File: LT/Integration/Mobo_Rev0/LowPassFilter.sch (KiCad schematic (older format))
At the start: 5 parts

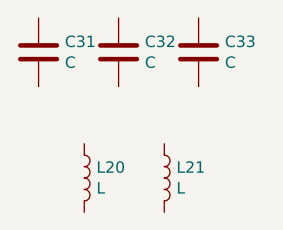
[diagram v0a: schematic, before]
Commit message: I uploaded the schematics for the receiving stage into their respective hierarchial sheets and have begun the integration of the received stage
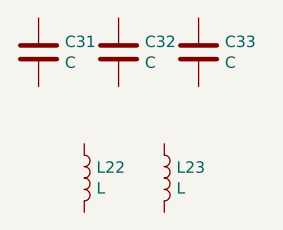
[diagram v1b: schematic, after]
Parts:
- C31, C32, C33: footprint Capacitor_SMD:C_0805_2012Metric -> (none)
- L22: renamed from L20; footprint Inductor_SMD:L_0805_2012Metric -> (none)
- L23: renamed from L21; footprint Inductor_SMD:L_0805_2012Metric -> (none)
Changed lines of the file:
@@
 F 0 "C31" H 4215 1946 50  0000 L CNN
 F 1 "C" H 4215 1855 50  0000 L CNN
-F 2 "Capacitor_SMD:C_0805_2012Metric" H 4138 1750 50  0001 C CNN
+F 2 "" H 4138 1750 50  0001 C CNN
 F 3 "~" H 4100 1900 50  0001 C CNN
 	1    4100 1900
@@
 F 0 "C32" H 4565 1946 50  0000 L CNN
 F 1 "C" H 4565 1855 50  0000 L CNN
-F 2 "Capacitor_SMD:C_0805_2012Metric" H 4488 1750 50  0001 C CNN
+F 2 "" H 4488 1750 50  0001 C CNN
 F 3 "~" H 4450 1900 50  0001 C CNN
 	1    4450 1900
@@
 F 0 "C33" H 4915 1946 50  0000 L CNN
 F 1 "C" H 4915 1855 50  0000 L CNN
-F 2 "Capacitor_SMD:C_0805_2012Metric" H 4838 1750 50  0001 C CNN
+F 2 "" H 4838 1750 50  0001 C CNN
 F 3 "~" H 4800 1900 50  0001 C CNN
 	1    4800 1900
@@
 $EndComp
 $Comp
-L Device:L L20
+L Device:L L22
 U 1 1 5E4C472F
 P 4300 2450
-F 0 "L20" H 4353 2496 50  0000 L CNN
+F 0 "L22" H 4353 2496 50  0000 L CNN
 F 1 "L" H 4353 2405 50  0000 L CNN
-F 2 "Inductor_SMD:L_0805_2012Metric" H 4300 2450 50  0001 C CNN
+F 2 "" H 4300 2450 50  0001 C CNN
 F 3 "~" H 4300 2450 50  0001 C CNN
 	1    4300 2450
@@
 $EndComp
 $Comp
-L Device:L L21
+L Device:L L23
 U 1 1 5E4C477A
 P 4650 2450
-F 0 "L21" H 4703 2496 50  0000 L CNN
+F 0 "L23" H 4703 2496 50  0000 L CNN
 F 1 "L" H 4703 2405 50  0000 L CNN
-F 2 "Inductor_SMD:L_0805_2012Metric" H 4650 2450 50  0001 C CNN
+F 2 "" H 4650 2450 50  0001 C CNN
 F 3 "~" H 4650 2450 50  0001 C CNN
 	1    4650 2450

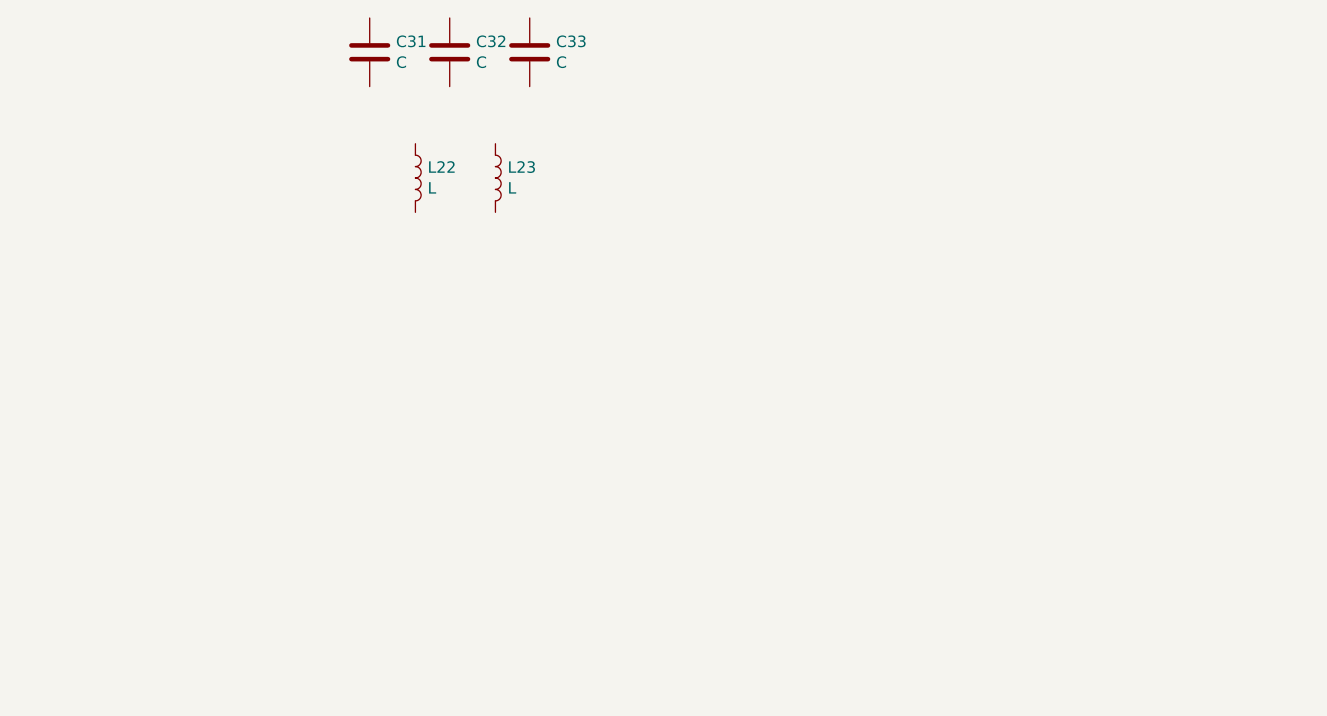
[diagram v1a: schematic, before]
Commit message: Finished a preliminary layout for the Receiving Stage, and uploaded the schematics for the Pre-Amp, 29.4 BPF, and 29.4 LPF.
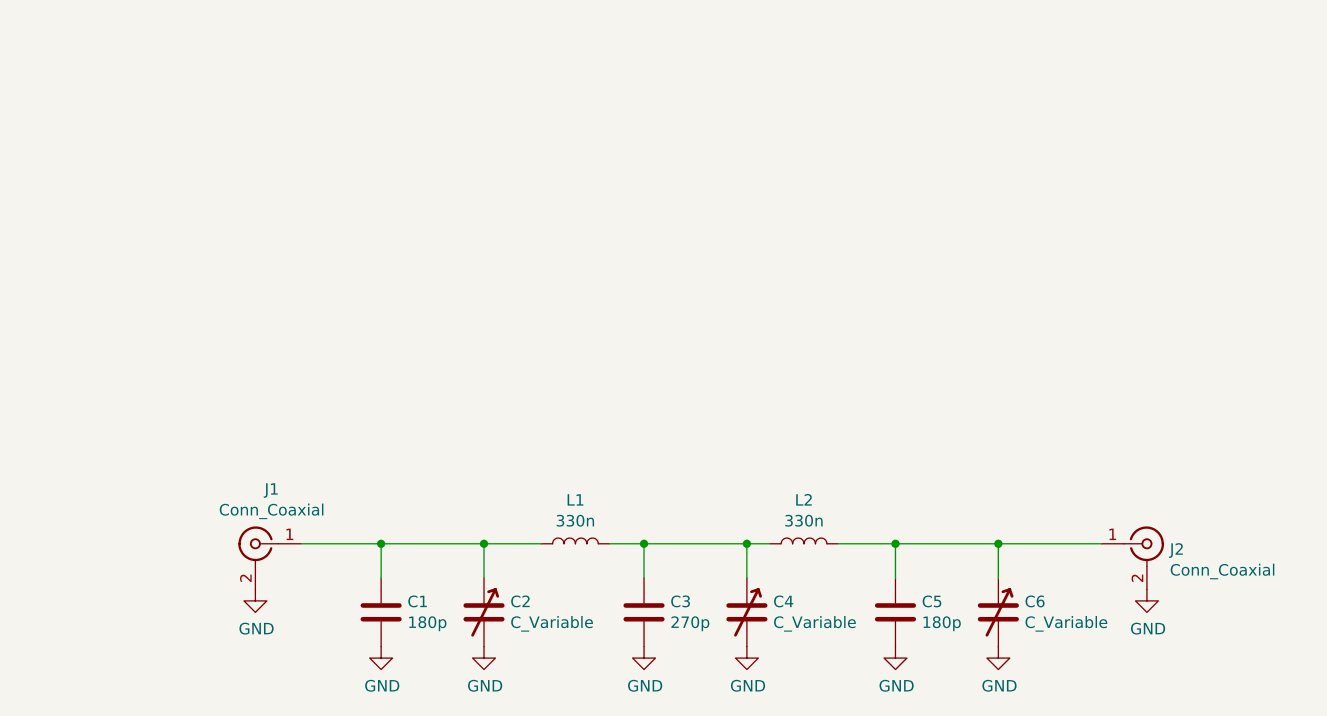
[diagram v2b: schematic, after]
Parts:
- removed C31, C32, C33: C, symbol Device:C
- removed L22, L23: L, symbol Device:L
- added C1, C5: 180p, Capacitor_SMD:C_0805_2012Metric_Pad1.15x1.40mm_HandSolder, symbol Device:C
- added C2, C4, C6: C_Variable, LT:CAP_Trimmer_TZB4Z, symbol Device:C_Variable
- added C3: 270p, Capacitor_SMD:C_0805_2012Metric_Pad1.15x1.40mm_HandSolder, symbol Device:C
- added J1, J2: Conn_Coaxial, Connector_Coaxial:SMA_Molex_73251-1153_EdgeMount_Horizontal, symbol Connector:Conn_Coaxial
- added L1, L2: 330n, Inductor_SMD:L_0805_2012Metric_Pad1.15x1.40mm_HandSolder, symbol Device:L
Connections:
- new net: C1.1, C2.1, J1.1 (In), L1.1
- new net: C3.1, C4.1, L1.2, L2.1
- new net: C5.1, C6.1, J2.1 (In), L2.2
- new net GND: C1.2, C2.2, C3.2, C4.2, C5.2, C6.2, J1.2 (Ext), J2.2 (Ext)

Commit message: Annotating components for Transmitting stage. In progress
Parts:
- renumbered C1 to C40, C2 to C41, C3 to C42, C4 to C43, C5 to C44, C6 to C45
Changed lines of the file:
@@
 $EndComp
 $Comp
-L Device:C C1
+L Device:C C40
 U 1 1 5E1FE5C6
 P 4150 4350
-F 0 "C1" H 4265 4396 50  0000 L CNN
+F 0 "C40" H 4265 4396 50  0000 L CNN
 F 1 "180p" H 4265 4305 50  0000 L CNN
 F 2 "Capacitor_SMD:C_0805_2012Metric_Pad1.15x1.40mm_HandSolder" H 4188 4200 50  0001 C CNN
@@
 $EndComp
 $Comp
-L Device:C C3
+L Device:C C42
 U 1 1 5E201B6F
 P 5300 4350
-F 0 "C3" H 5415 4396 50  0000 L CNN
+F 0 "C42" H 5415 4396 50  0000 L CNN
 F 1 "270p" H 5415 4305 50  0000 L CNN
 F 2 "Capacitor_SMD:C_0805_2012Metric_Pad1.15x1.40mm_HandSolder" H 5338 4200 50  0001 C CNN
@@
 $EndComp
 $Comp
-L Device:C C5
+L Device:C C44
 U 1 1 5E202B59
 P 6400 4350
-F 0 "C5" H 6515 4396 50  0000 L CNN
+F 0 "C44" H 6515 4396 50  0000 L CNN
 F 1 "180p" H 6515 4305 50  0000 L CNN
 F 2 "Capacitor_SMD:C_0805_2012Metric_Pad1.15x1.40mm_HandSolder" H 6438 4200 50  0001 C CNN
@@
 $EndComp
 $Comp
-L Device:C_Variable C2
+L Device:C_Variable C41
 U 1 1 5E2046E0
 P 4600 4350
-F 0 "C2" H 4715 4396 50  0000 L CNN
+F 0 "C41" H 4715 4396 50  0000 L CNN
 F 1 "C_Variable" H 4715 4305 50  0000 L CNN
 F 2 "LT:CAP_Trimmer_TZB4Z" H 4600 4350 50  0001 C CNN
@@
 Connection ~ 4150 4050
 $Comp
-L Device:C_Variable C4
+L Device:C_Variable C43
 U 1 1 5E2093F8
 P 5750 4350
-F 0 "C4" H 5865 4396 50  0000 L CNN
+F 0 "C43" H 5865 4396 50  0000 L CNN
 F 1 "C_Variable" H 5865 4305 50  0000 L CNN
 F 2 "LT:CAP_Trimmer_TZB4Z" H 5750 4350 50  0001 C CNN
@@
 $EndComp
 $Comp
-L Device:C_Variable C6
+L Device:C_Variable C45
 U 1 1 5E20A887
 P 6850 4350
-F 0 "C6" H 6965 4396 50  0000 L CNN
+F 0 "C45" H 6965 4396 50  0000 L CNN
 F 1 "C_Variable" H 6965 4305 50  0000 L CNN
 F 2 "LT:CAP_Trimmer_TZB4Z" H 6850 4350 50  0001 C CNN

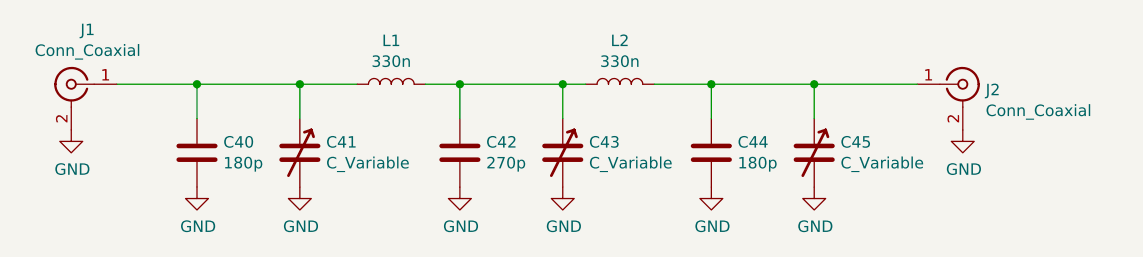
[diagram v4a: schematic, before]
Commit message: Transmitting stage annotations are done. Ready to layout PCB for rev0
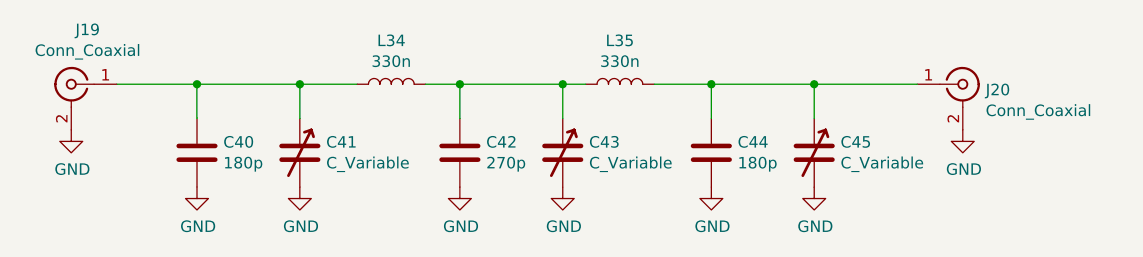
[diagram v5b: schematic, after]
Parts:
- renumbered J1 to J19, J2 to J20, L1 to L34, L2 to L35
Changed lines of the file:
@@
 $EndDescr
 $Comp
-L Connector:Conn_Coaxial J1
+L Connector:Conn_Coaxial J19
 U 1 1 5E1FC498
 P 3600 4050
-F 0 "J1" H 3528 4288 50  0000 C CNN
+F 0 "J19" H 3528 4288 50  0000 C CNN
 F 1 "Conn_Coaxial" H 3528 4197 50  0000 C CNN
 F 2 "Connector_Coaxial:SMA_Molex_73251-1153_EdgeMount_Horizontal" H 3600 4050 50  0001 C CNN
@@
 $EndComp
 $Comp
-L Device:L L1
+L Device:L L34
 U 1 1 5E1FED39
 P 5000 4050
-F 0 "L1" V 5190 4050 50  0000 C CNN
+F 0 "L34" V 5190 4050 50  0000 C CNN
 F 1 "330n" V 5099 4050 50  0000 C CNN
 F 2 "Inductor_SMD:L_0805_2012Metric_Pad1.15x1.40mm_HandSolder" H 5000 4050 50  0001 C CNN
@@
 $EndComp
 $Comp
-L Device:L L2
+L Device:L L35
 U 1 1 5E201B79
 P 6000 4050
-F 0 "L2" V 6190 4050 50  0000 C CNN
+F 0 "L35" V 6190 4050 50  0000 C CNN
 F 1 "330n" V 6099 4050 50  0000 C CNN
 F 2 "Inductor_SMD:L_0805_2012Metric_Pad1.15x1.40mm_HandSolder" H 6000 4050 50  0001 C CNN
@@
 $EndComp
 $Comp
-L Connector:Conn_Coaxial J2
+L Connector:Conn_Coaxial J20
 U 1 1 5E20B5B6
 P 7500 4050
-F 0 "J2" H 7600 4025 50  0000 L CNN
+F 0 "J20" H 7600 4025 50  0000 L CNN
 F 1 "Conn_Coaxial" H 7600 3934 50  0000 L CNN
 F 2 "Connector_Coaxial:SMA_Molex_73251-1153_EdgeMount_Horizontal" H 7500 4050 50  0001 C CNN

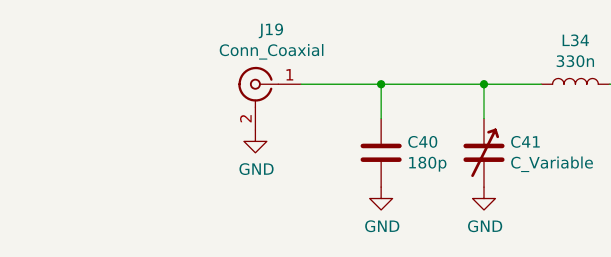
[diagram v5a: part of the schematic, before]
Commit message: Working on Transmitting Stage rev 0 integration board. Still in progress
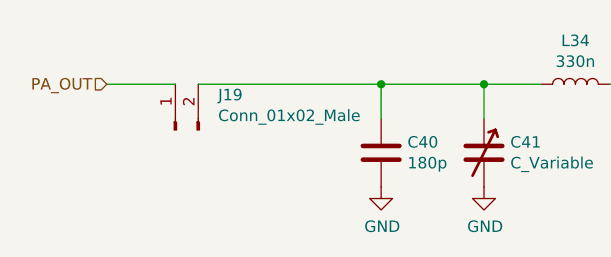
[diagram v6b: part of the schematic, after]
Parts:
- removed J19: Conn_Coaxial, Connector_Coaxial:SMA_Molex_73251-1153_EdgeMount_Horizontal, symbol Connector:Conn_Coaxial
- added J19: Conn_01x02_Male, Connector_PinHeader_2.54mm:PinHeader_1x02_P2.54mm_Vertical, symbol Connector:Conn_01x02_Male
- J20: footprint Connector_Coaxial:SMA_Molex_73251-1153_EdgeMount_Horizontal -> Connector_Coaxial:SMA_Amphenol_132289_EdgeMount
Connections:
- net at C40.1, C41.1, L34.1: now also J19.2 (Pin_2)
- new net PA_OUT: J19.1 (Pin_1)
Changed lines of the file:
@@
 $EndDescr
-$Comp
-L Connector:Conn_Coaxial J19
-U 1 1 5E1FC498
-P 3600 4050
-F 0 "J19" H 3528 4288 50  0000 C CNN
-F 1 "Conn_Coaxial" H 3528 4197 50  0000 C CNN
-F 2 "Connector_Coaxial:SMA_Molex_73251-1153_EdgeMount_Horizontal" H 3600 4050 50  0001 C CNN
-F 3 " ~" H 3600 4050 50  0001 C CNN
-	1    3600 4050
-	-1   0    0    -1
-$EndComp
 $Comp
 L Device:C C40
@@
 $EndComp
 Wire Wire Line
-	3800 4050 4150 4050
-Wire Wire Line
 	5150 4050 5300 4050
 Wire Wire Line
@@
 Wire Wire Line
 	4150 4200 4150 4050
-$Comp
-L power:GND #PWR0113
-U 1 1 5E2035DD
-P 3600 4250
-F 0 "#PWR0113" H 3600 4000 50  0001 C CNN
-F 1 "GND" H 3605 4077 50  0000 C CNN
-F 2 "" H 3600 4250 50  0001 C CNN
-F 3 "" H 3600 4250 50  0001 C CNN
-	1    3600 4250
-	1    0    0    -1
-$EndComp
 $Comp
 L power:GND #PWR0114
@@
 F 0 "J20" H 7600 4025 50  0000 L CNN
 F 1 "Conn_Coaxial" H 7600 3934 50  0000 L CNN
-F 2 "Connector_Coaxial:SMA_Molex_73251-1153_EdgeMount_Horizontal" H 7500 4050 50  0001 C CNN
+F 2 "Connector_Coaxial:SMA_Amphenol_132289_EdgeMount" H 7500 4050 50  0001 C CNN
 F 3 " ~" H 7500 4050 50  0001 C CNN
 	1    7500 4050
@@
 	4600 4050 4850 4050
 Connection ~ 5750 4050
+Text HLabel 2950 4050 0    50   Input ~ 0
+PA_OUT
+Wire Wire Line
+	2950 4050 3250 4050
+$Comp
+L Connector:Conn_01x02_Male J19
+U 1 1 5EA07F0D
+P 3250 4250
+F 0 "J19" V 3403 4063 50  0000 R CNN
+F 1 "Conn_01x02_Male" V 3312 4063 50  0000 R CNN
+F 2 "Connector_PinHeader_2.54mm:PinHeader_1x02_P2.54mm_Vertical" H 3250 4250 50  0001 C CNN
+F 3 "~" H 3250 4250 50  0001 C CNN
+	1    3250 4250
+	0    -1   -1   0
+$EndComp
+Wire Wire Line
+	3350 4050 4150 4050
 $EndSCHEMATC
